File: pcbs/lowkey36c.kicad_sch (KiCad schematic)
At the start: 76 parts

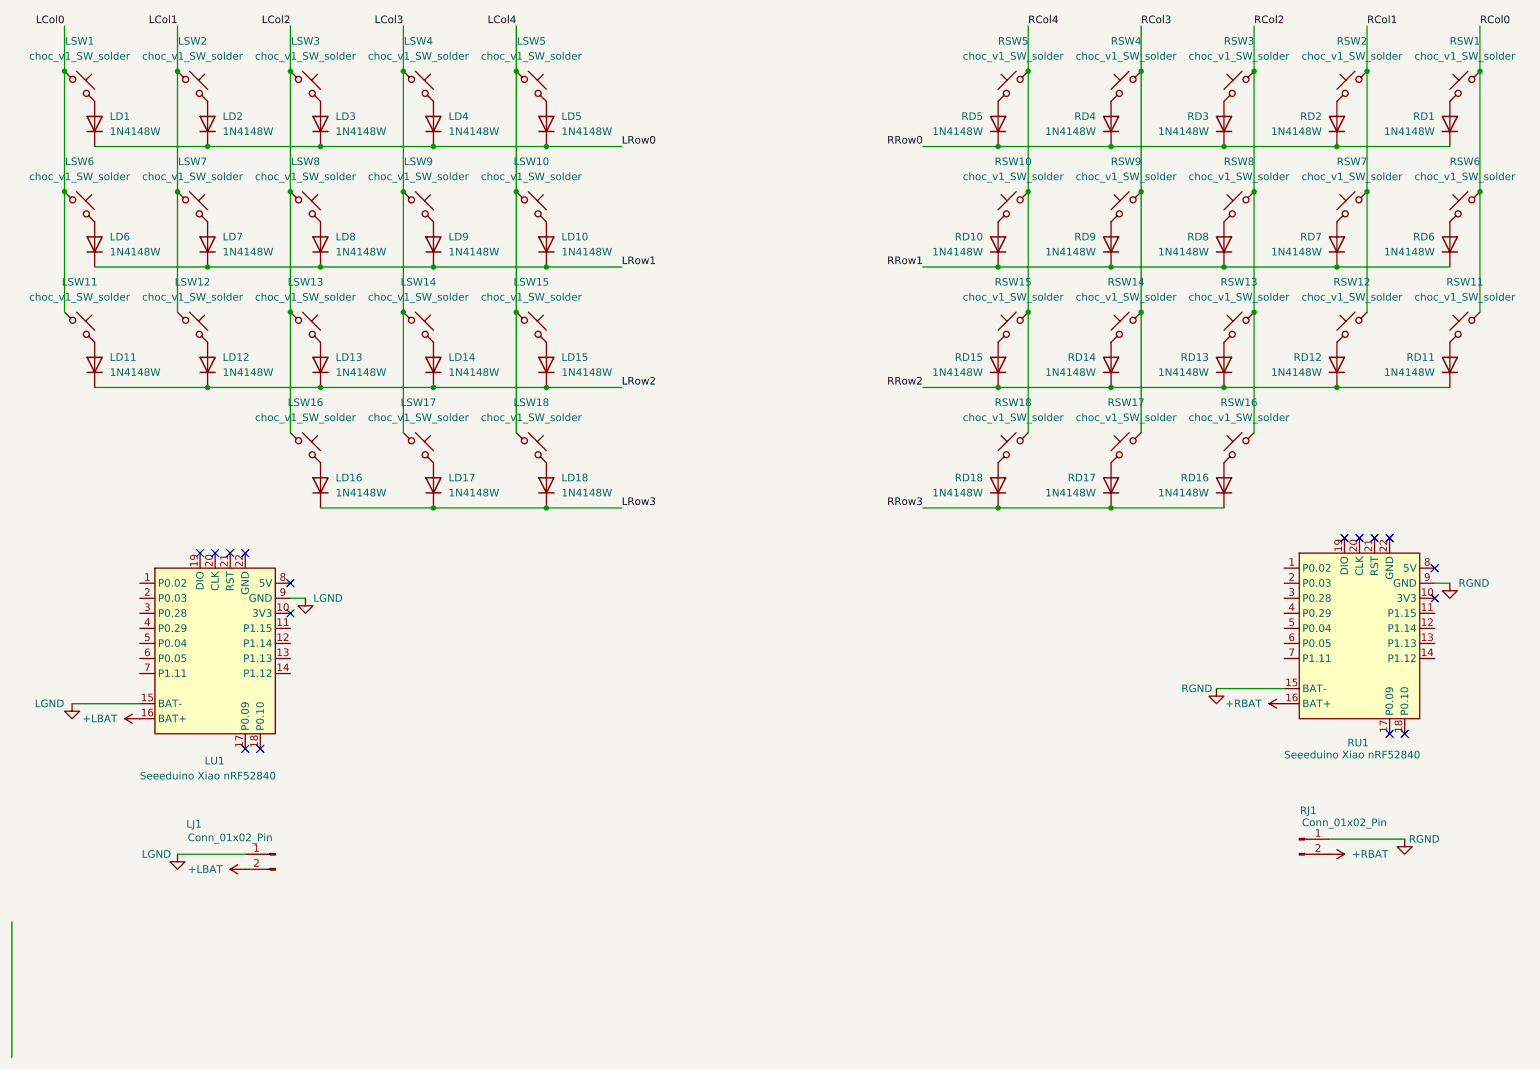
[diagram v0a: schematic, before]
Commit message: add component submodules and update pcb files
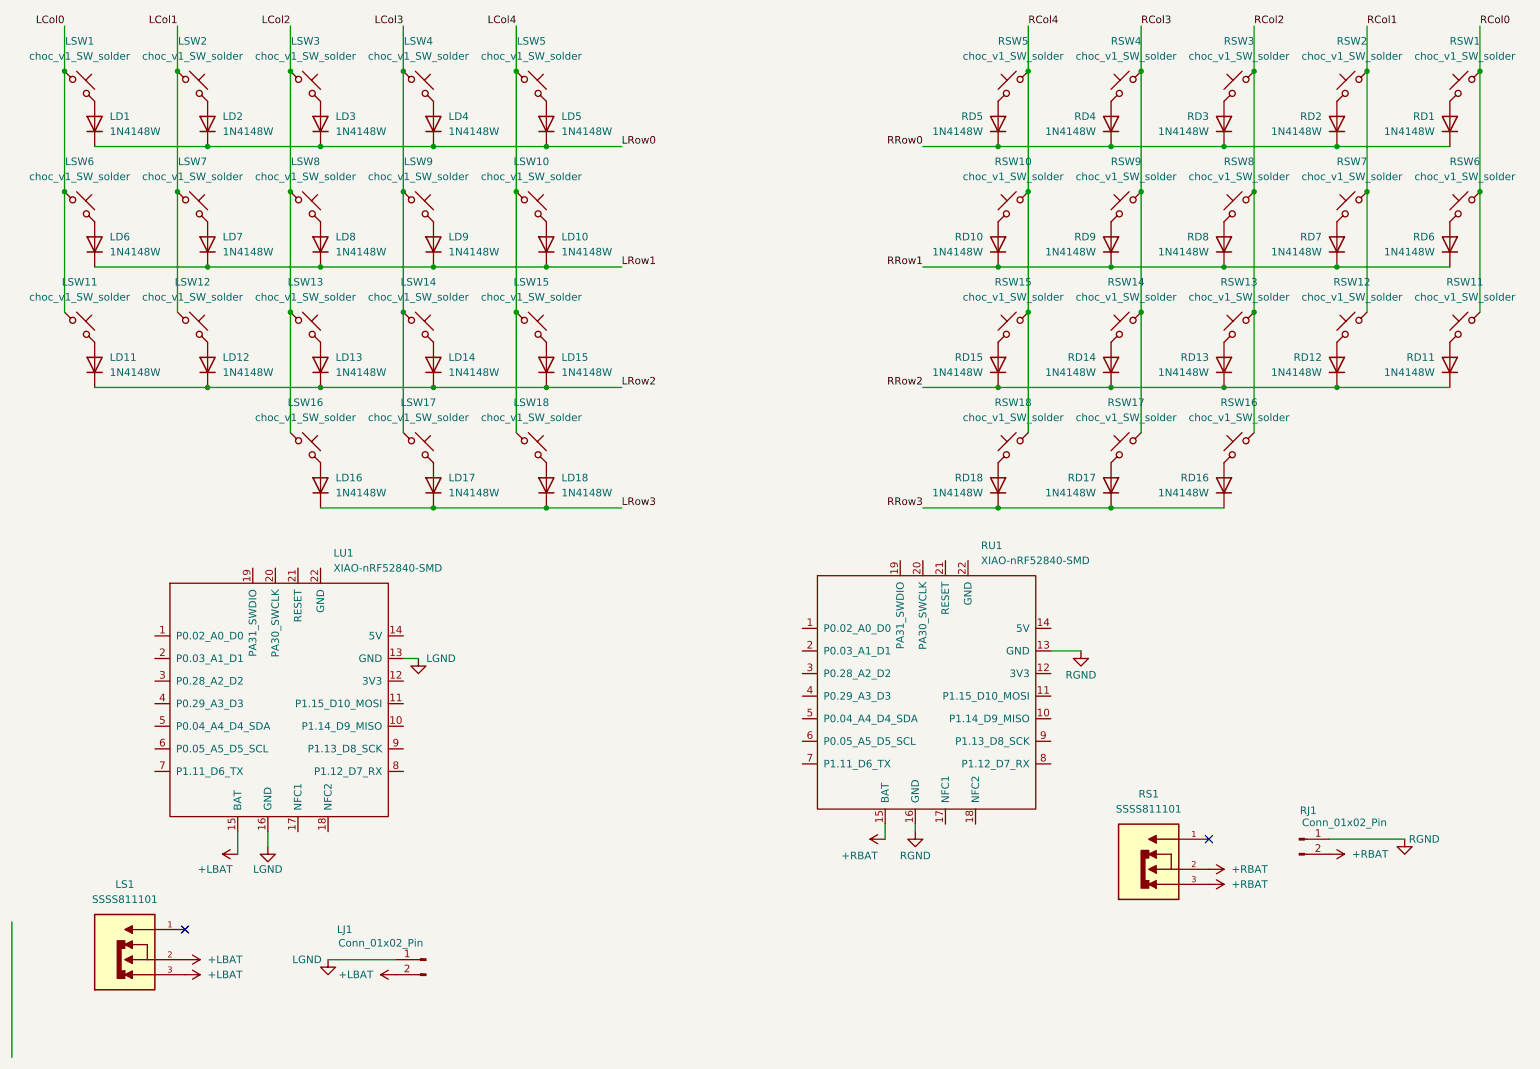
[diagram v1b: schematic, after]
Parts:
- removed LU1, RU1: Seeeduino Xiao nRF52840, PCM_marbastlib-xp-promicroish:Xiao_nRF52840_ACH, symbol PCM_marbastlib-promicroish:Seeeduino_Xiao_nRF52840
- added LS1, RS1: SSSS811101, mg_pwr_sw:SW_SSSS811101, symbol mg_pwr_sw:SSSS811101
- added LU1, RU1: XIAO-nRF52840-SMD, kleeb_mcu:xiao-ble-smd-cutout, symbol Seeed_Studio_XIAO_Series:XIAO-nRF52840-SMD
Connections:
- net +LBAT: now also LS1.2, LS1.3, LU1.15 (BAT)
- net +RBAT: now also RS1.2, RS1.3, RU1.15 (BAT)
- net LGND: now also LU1.13 (GND), LU1.16 (GND)
- net RGND: now also RU1.13 (GND), RU1.16 (GND)
- no-connect marks 16 -> 2
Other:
- moved on the sheet: LJ1
